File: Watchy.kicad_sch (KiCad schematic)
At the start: 73 parts, among them J1 FPC24(0.5MM), J2 USB_C_Receptacle_USB2.0, J3 Battery, M1 Vibration_Motor, Q1 AO3400A, Q2 UMH3N, Q4 CJ2301, Q5 S8050, SW1 BTN, SW2 BTN, SW3 BTN, SW4 BTN, U1 ESP32-PICO-D4, U2 ME6211C33M5G-N, U3 CP2102, U4 BMA423, U5 TP4054, U6 PCF8563BS, Y1 32.768KHz

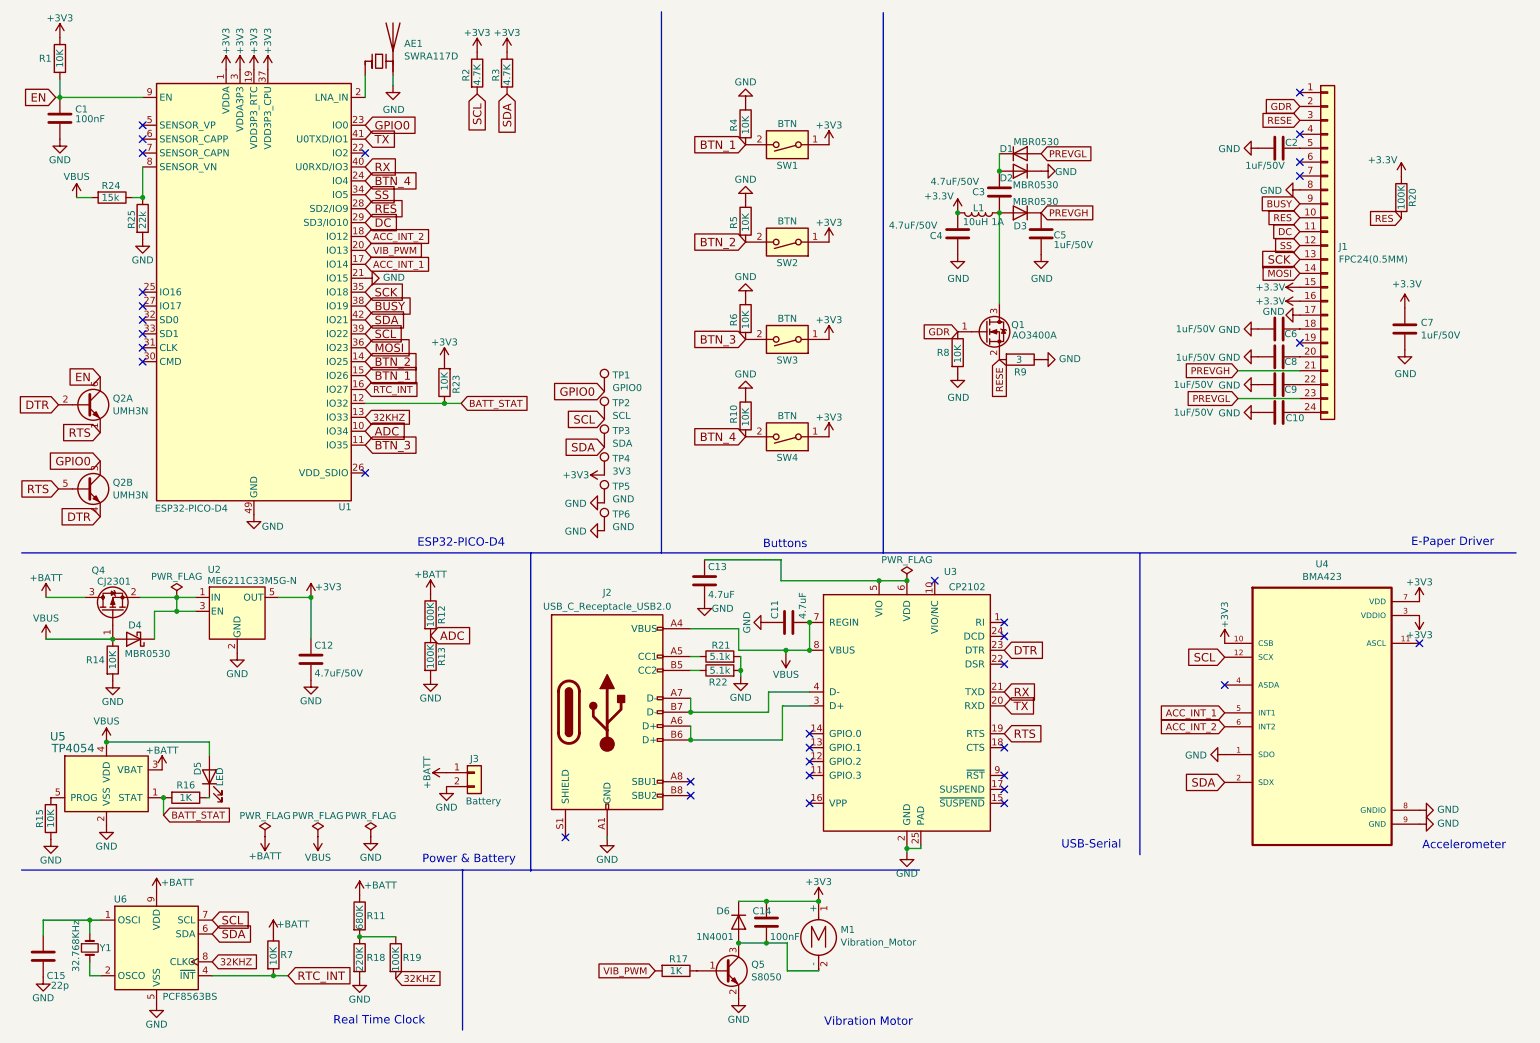
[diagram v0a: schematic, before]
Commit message: fixed flashing issue
Replaced 100nF enabled cap with 1uF
re-annotated parts
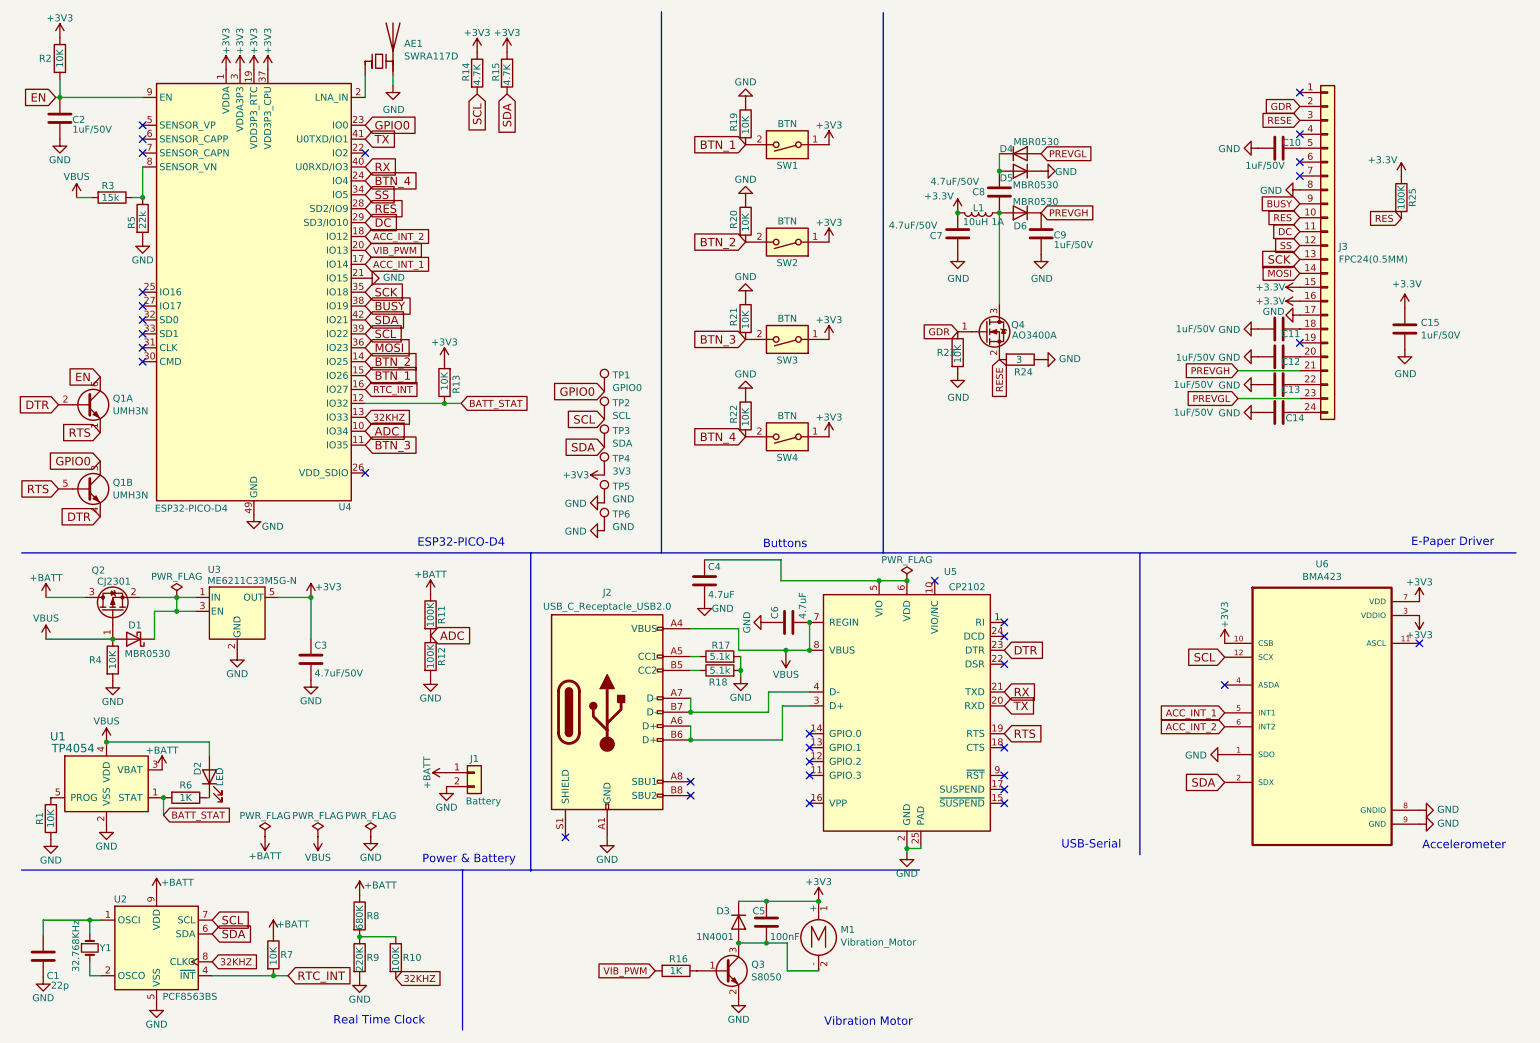
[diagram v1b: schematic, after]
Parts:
- removed C1: 100nF, Capacitor_SMD:C_0603_1608Metric, symbol Device:C
- added C2: 1uF/50V, Capacitor_SMD:C_0603_1608Metric, symbol Device:C
- renumbered C15 to C1, C2 to C10, C6 to C11, C8 to C12, C9 to C13, C10 to C14, C7 to C15, C12 to C3, C13 to C4, C14 to C5, C11 to C6, C4 to C7, C3 to C8, C5 to C9, D4 to D1, D5 to D2, D6 to D3, D1 to D4, D2 to D5, D3 to D6, J3 to J1, J1 to J3, Q2 to Q1, Q4 to Q2, Q5 to Q3, Q1 to Q4, R15 to R1, R19 to R10, R12 to R11, R13 to R12, R23 to R13, R2 to R14, R3 to R15, R17 to R16, R21 to R17, R22 to R18, R4 to R19, R1 to R2, R5 to R20, R6 to R21, R10 to R22, R8 to R23, R9 to R24, R20 to R25, R24 to R3, R14 to R4, R25 to R5, R16 to R6, R11 to R8, R18 to R9, U5 to U1, U6 to U2, U2 to U3, U1 to U4, U3 to U5, U4 to U6
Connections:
- net EN: now also C2.1
- net GND: now also C2.2

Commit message: Revert "fixed flashing issue"
This reverts commit 310c791037fab022fc14582fc30034d46f66ed13.
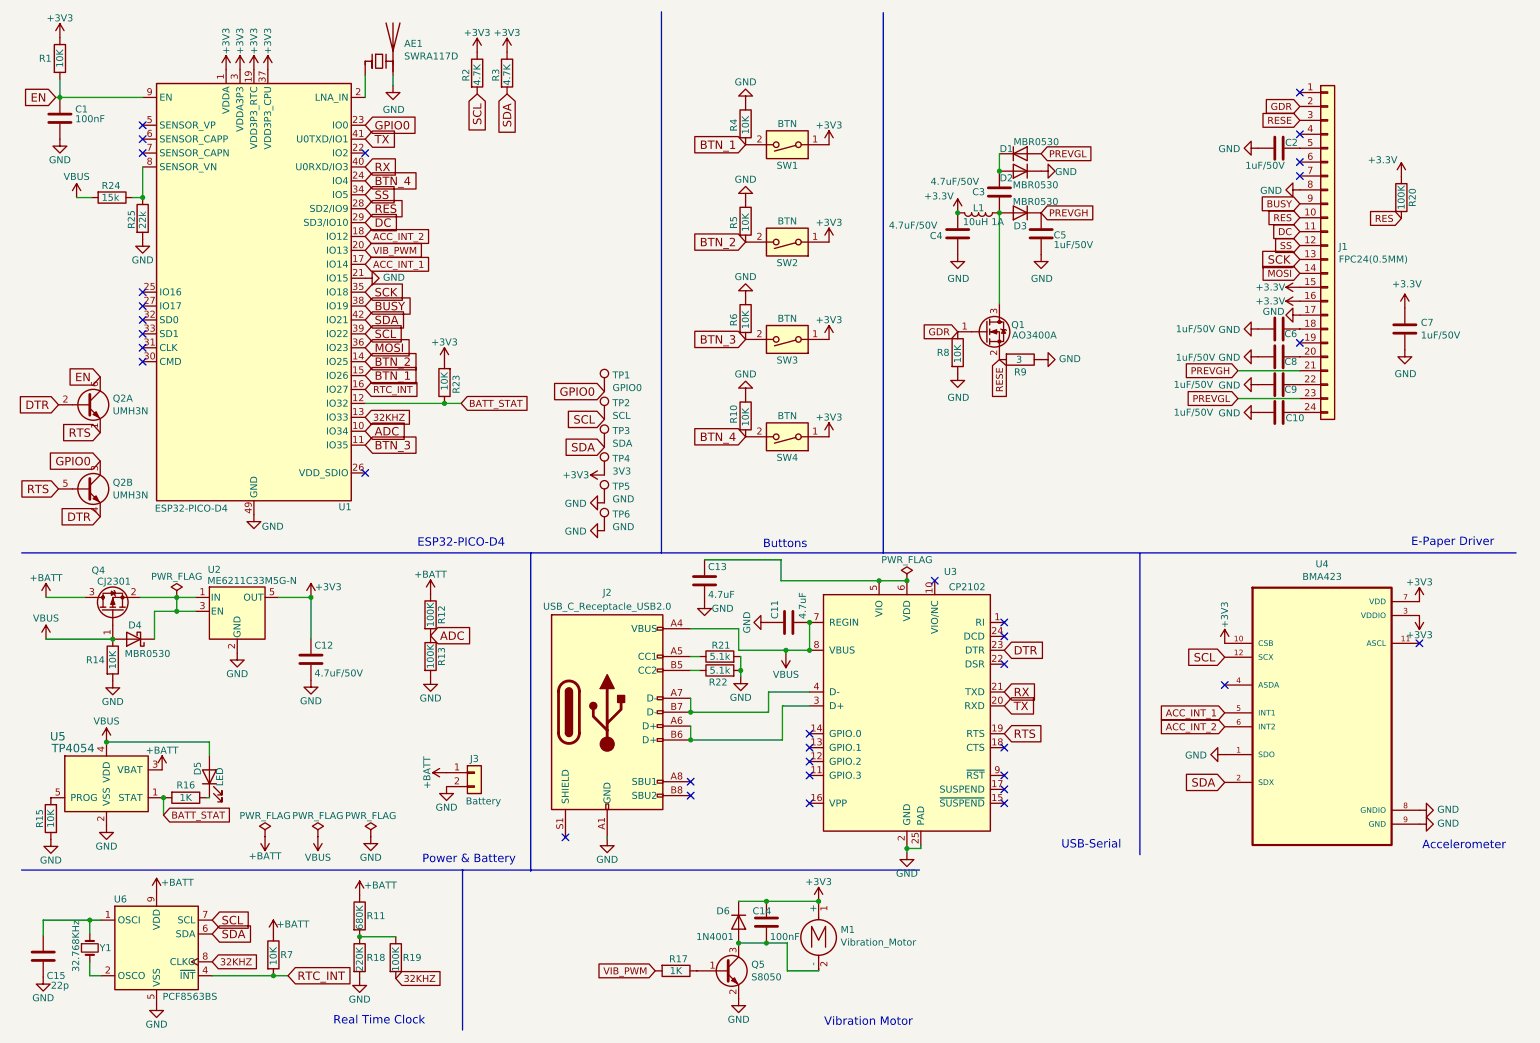
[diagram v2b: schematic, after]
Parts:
- removed C2: 1uF/50V, Capacitor_SMD:C_0603_1608Metric, symbol Device:C
- added C1: 100nF, Capacitor_SMD:C_0603_1608Metric, symbol Device:C
- renumbered C14 to C10, C6 to C11, C3 to C12, C4 to C13, C5 to C14, C1 to C15, C10 to C2, C8 to C3, C7 to C4, C9 to C5, C11 to C6, C15 to C7, C12 to C8, C13 to C9, D4 to D1, D5 to D2, D6 to D3, D1 to D4, D2 to D5, D3 to D6, J3 to J1, J1 to J3, Q4 to Q1, Q1 to Q2, Q2 to Q4, Q3 to Q5, R2 to R1, R22 to R10, R8 to R11, R11 to R12, R12 to R13, R4 to R14, R1 to R15, R6 to R16, R16 to R17, R9 to R18, R10 to R19, R14 to R2, R25 to R20, R17 to R21, R18 to R22, R13 to R23, R3 to R24, R5 to R25, R15 to R3, R19 to R4, R20 to R5, R21 to R6, R23 to R8, R24 to R9, U4 to U1, U3 to U2, U5 to U3, U6 to U4, U1 to U5, U2 to U6
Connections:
- net EN: now also C1.1
- net GND: now also C1.2
